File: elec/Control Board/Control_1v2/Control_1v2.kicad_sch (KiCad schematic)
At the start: 170 parts, among them J1 DB9_Female_MountingHoles, J10 Conn_02x12_Odd_Even, J11 Con_01x02_2.5mm, J14 Conn_01x10, J2 Conn_01x08, J25 Con_01x02_2.5mm, J26 Conn_01x10, J27 Conn_02x12_Odd_Even, J28 Con_01x02_2.5mm, J29 Conn_01x10, J3 Conn_01x08, J37 Conn_01x04, J4 Conn_01x08, J5 Conn_01x08, J6 Conn_01x08, J7 Conn_01x10, J8 Conn_02x18_Odd_Even, J9 Conn_01x10, Q601 BSS138

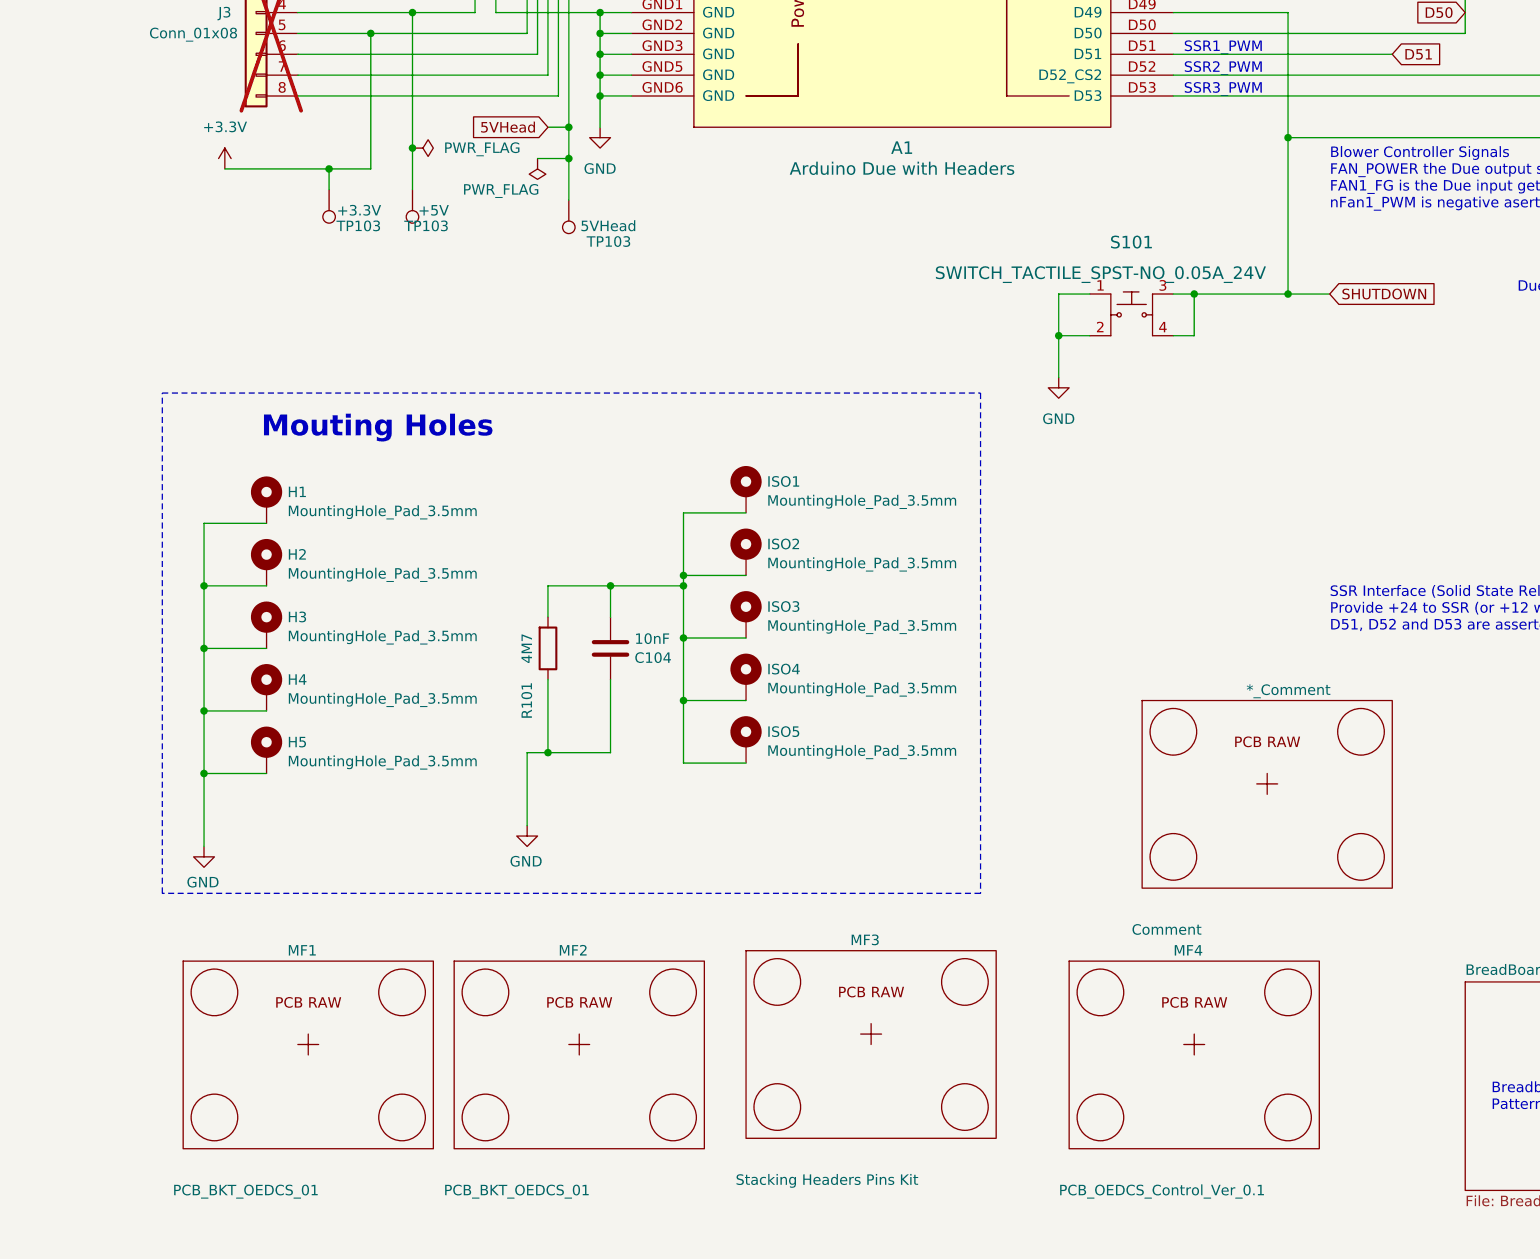
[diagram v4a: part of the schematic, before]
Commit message: Add a connector next to the SHUTDOWN switch. Add 3D file for relay.
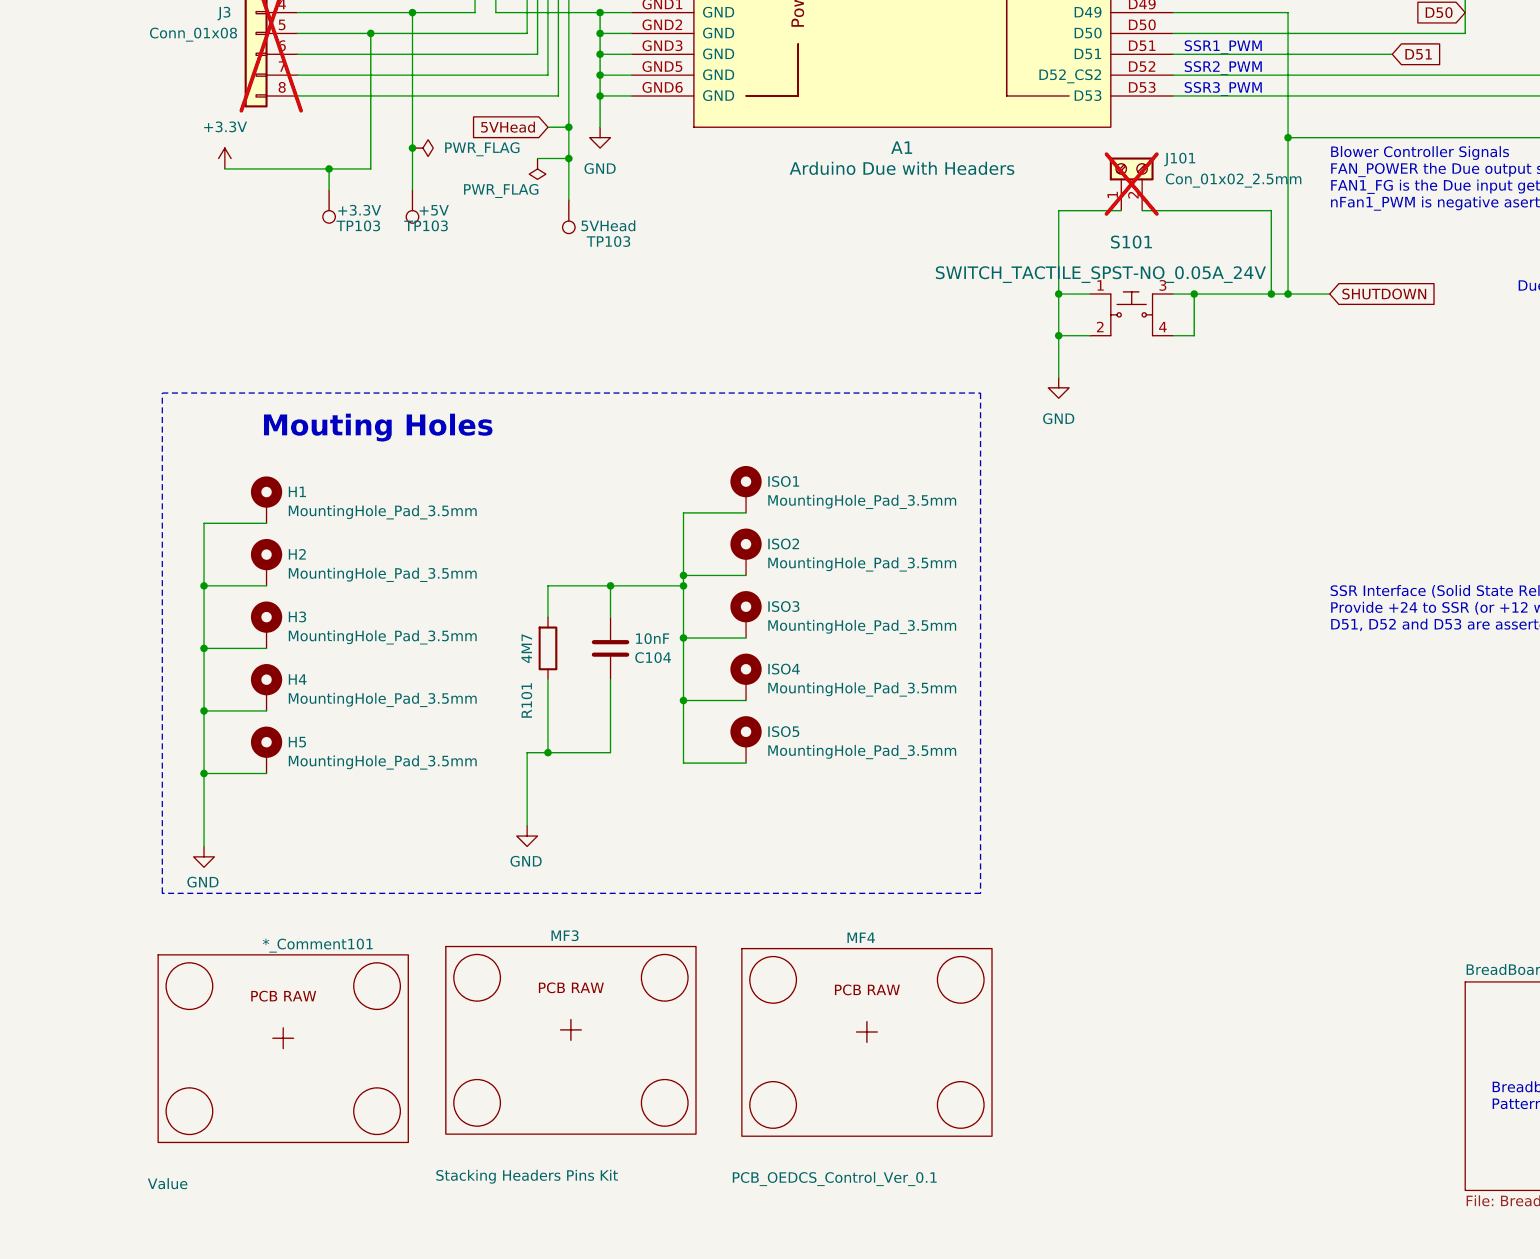
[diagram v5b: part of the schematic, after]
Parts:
- removed MF1, MF2: PCB_BKT_OEDCS_01, NA, symbol GPAD_SCH_LIB:PCB_GPAD_VER1
- added J101: Con_01x02_2.5mm, PubInv_KiCad_PCB:JST_XH_B2B-XH-AM_1x02_P2.50mm_Vertical, symbol Connector:Screw_Terminal_01x02
- *_Comment101: renamed from *_Comment; value Comment -> Value
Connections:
- net GND: now also J101.1 (Pin_1)
- net SHUTDOWN: now also J101.2 (Pin_2)
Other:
- moved on the sheet: *_Comment101, MF3, MF4

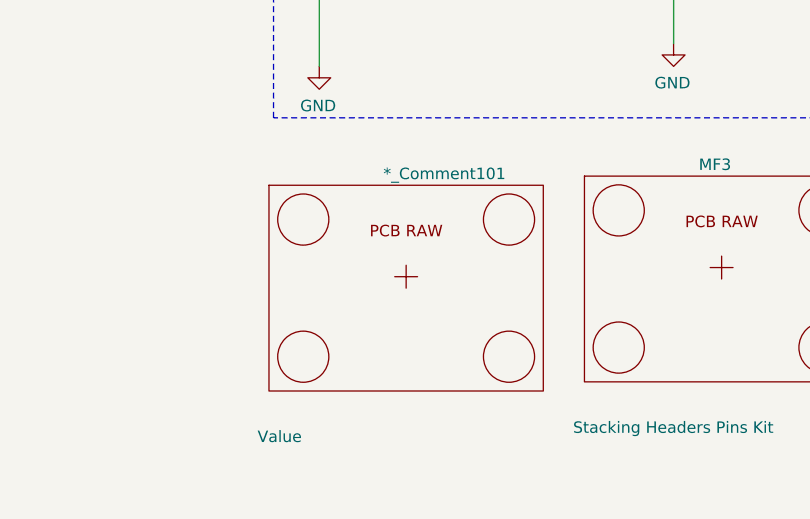
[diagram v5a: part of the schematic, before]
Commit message: PCB V1.2. Fixes to parts for BOM and PL.
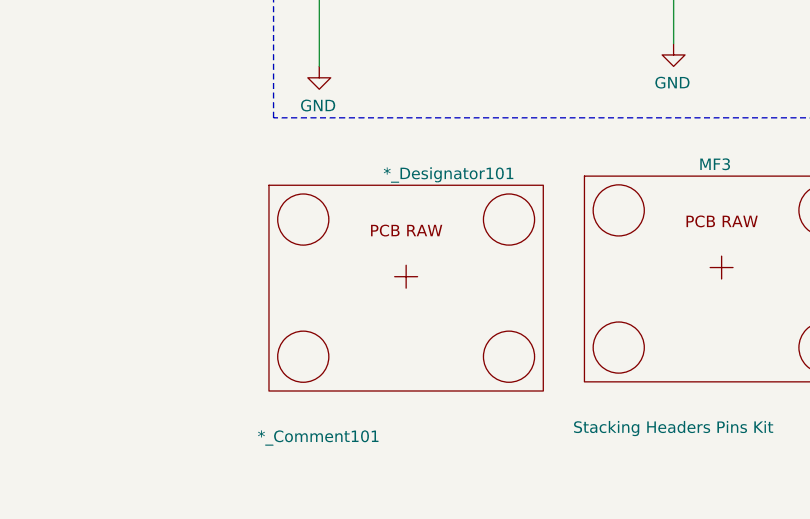
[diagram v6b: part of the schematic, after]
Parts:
- *_Designator101: renamed from *_Comment101; value Value -> *_Comment101
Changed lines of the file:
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@@
   (symbol (lib_id "GPAD_SCH_LIB:PCB_GPAD_VER1") (at 174.752 290.068 0) (unit 1)
     (in_bom yes) (on_board no) (dnp no)
-    (property "Reference" "*_Comment101" (at 172.212 278.638 0)
+    (property "Reference" "*_Designator101" (at 172.212 278.638 0)
       (effects (font (size 1.27 1.27)) (justify left))
     )
-    (property "Value" "Value" (at 158.242 307.848 0)
+    (property "Value" "*_Comment101" (at 158.242 307.848 0)
       (effects (font (size 1.27 1.27)) (justify left))
     )
@@
       (project "Control_1v2"
         (path "/c68c9deb-8d4d-42f0-adf8-4d3022f4ee59"
-          (reference "*_Comment101") (unit 1)
+          (reference "*_Designator101") (unit 1)
         )
       )

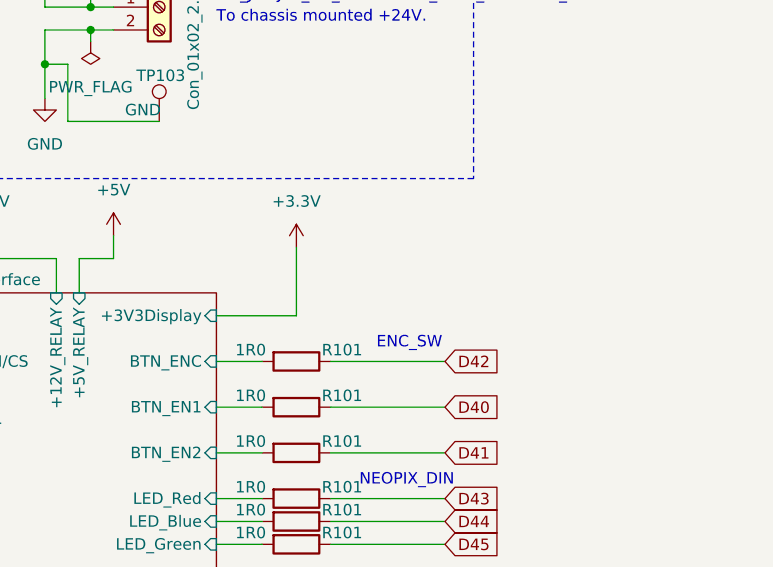
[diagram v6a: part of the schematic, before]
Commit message: Update schematic with new resistor R186 required for front panel switch.
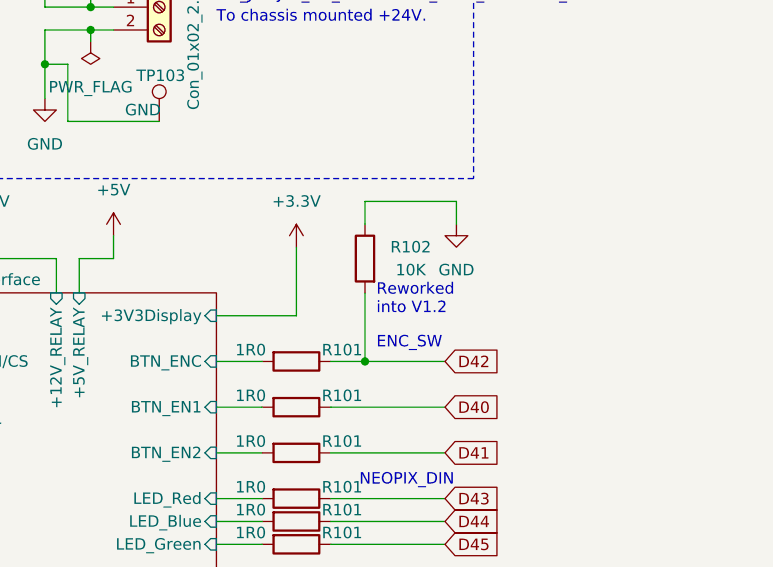
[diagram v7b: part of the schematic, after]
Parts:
- added R102: 10K, Resistor_SMD:R_0603_1608Metric_Pad0.98x0.95mm_HandSolder, symbol Device:R
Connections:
- net D42: now also R102.2
- net GND: now also R102.1
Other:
- note added: "Reworked into V1.2"
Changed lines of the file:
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@@
   (junction (at 213.36 167.64) (diameter 0) (color 0 0 0 0)
   )
+  (junction (at 505.46 246.38) (diameter 0) (color 0 0 0 0)
+  )
   (junction (at 477.52 132.08) (diameter 0) (color 0 0 0 0)
   )
@@
     (stroke (width 0) (type default))
   )
+  (wire (pts (xy 515.62 228.6) (xy 505.46 228.6))
+    (stroke (width 0) (type default))
+  )
   (wire (pts (xy 426.72 50.8) (xy 424.18 50.8))
     (stroke (width 0) (type default))
@@
     (stroke (width 0) (type default))
   )
+  (wire (pts (xy 505.46 228.6) (xy 505.46 231.14))
+    (stroke (width 0) (type default))
+  )
   (wire (pts (xy 463.55 91.44) (xy 463.55 114.3))
     (stroke (width 0) (type default))
@@
     (stroke (width 0) (type default))
   )
-  (wire (pts (xy 514.35 246.38) (xy 501.65 246.38))
+  (wire (pts (xy 514.35 246.38) (xy 505.46 246.38))
     (stroke (width 0) (type default))
   )
@@
     (stroke (width 0) (type default))
   )
+  (wire (pts (xy 515.62 231.14) (xy 515.62 228.6))
+    (stroke (width 0) (type default))
+  )
   (wire (pts (xy 477.52 127) (xy 455.93 127))
     (stroke (width 0) (type default))
@@
     (stroke (width 0) (type default))
   )
+  (wire (pts (xy 505.46 246.38) (xy 501.65 246.38))
+    (stroke (width 0) (type default))
+  )
   (wire (pts (xy 448.31 246.38) (xy 454.66 246.38))
     (stroke (width 0) (type default))
@@
     (stroke (width 0) (type default))
   )
+  (wire (pts (xy 505.46 238.76) (xy 505.46 246.38))
+    (stroke (width 0) (type default))
+  )
   (wire (pts (xy 433.07 49.53) (xy 426.72 49.53))
     (stroke (width 0) (type default))
@@
     (effects (font (size 1.27 1.27)) (justify left bottom))
   )
+  (text "Reworked \ninto V1.2" (at 506.73 241.3 0)
+    (effects (font (size 1.27 1.27)) (justify left bottom))
+  )
   (text "V_ASSY_VERSIONING\nControl 1.2 voltage = 1.055V" (at 124.714 137.414 0)
     (effects (font (size 1.27 1.27)) (justify left bottom))
@@
     )
   )
+  (symbol (lib_id "Device:R") (at 505.46 234.95 0) (mirror y) (unit 1)
+    (in_bom yes) (on_board yes) (dnp no)
+    (property "Reference" "R102" (at 510.54 233.68 0)
+      (effects (font (size 1.27 1.27)))
+    )
+    (property "Value" "10K" (at 510.54 236.22 0)
+      (effects (font (size 1.27 1.27)))
+    )
+    (property "Footprint" "Resistor_SMD:R_0603_1608Metric_Pad0.98x0.95mm_HandSolder" (at 507.238 234.95 90)
+      (effects (font (size 1.27 1.27)) hide)
+    )
+    (property "Datasheet" "https://datasheet.lcsc.com/lcsc/1811101310_TyoHM-RMC06031K1-N_C269704.pdf" (at 505.46 234.95 0)
+      (effects (font (size 1.27 1.27)) hide)
+    )
+    (property "Distributor 1" "JLCPCB" (at 505.46 234.95 90)
+      (effects (font (size 1.27 1.27)) hide)
+    )
+    (property "Distributor 1 PN" "C269701" (at 505.46 234.95 90)
+      (effects (font (size 1.27 1.27)) hide)
+    )
+    (property "Manufacturer" "TyoHM" (at 505.46 234.95 90)
+      (effects (font (size 1.27 1.27)) hide)
+    )
+    (property "MPN" "RMC060310KFN" (at 505.46 234.95 90)
+      (effects (font (size 1.27 1.27)) hide)
+    )
+    (property "Description" "100mW ±1% 10kΩ 0603 Chip Resistor - Surface Mount ROHS" (at 505.46 234.95 0)
+      (effects (font (size 1.27 1.27)) hide)
+    )
+    (property "AssemblyType" "SMT" (at 505.46 234.95 0)
+      (effects (font (size 1.27 1.27)) hide)
+    )
+    (property "Cost" "0.0015" (at 505.46 234.95 0)
+      (effects (font (size 1.27 1.27)) hide)
+    )
+    (property "LongLead" "NO" (at 505.46 234.95 0)
+      (effects (font (size 1.27 1.27)) hide)
+    )
+    (pin "1")
+    (pin "2")
+    (instances
+      (project "GeneralPurposeAlarmDevicePCB"
+        (path "/412a327d-1ee3-473e-bc00-1545004b7edf"
+          (reference "R102") (unit 1)
+        )
+      )
+      (project "Control_1v2"
+        (path "/c68c9deb-8d4d-42f0-adf8-4d3022f4ee59/0cb2f0dc-fe38-451d-b752-5d12a98f8d03"
+          (reference "R41") (unit 1)
+        )
+        (path "/c68c9deb-8d4d-42f0-adf8-4d3022f4ee59"
+          (reference "R186") (unit 1)
+        )
+      )
+    )
+  )
   (symbol (lib_id "Device:R") (at 80.01 285.75 180) (unit 1)
     (in_bom yes) (on_board yes) (dnp no)
@@
         )
       )
+    )
+  )
+  (symbol (lib_id "power:GND") (at 515.62 231.14 0) (unit 1)
+    (in_bom yes) (on_board yes) (dnp no) (fields_autoplaced)
+    (property "Reference" "#PWR0113" (at 515.62 237.49 0)
+      (effects (font (size 1.27 1.27)) hide)
+    )
+    (property "Value" "GND" (at 515.62 236.22 0)
+      (effects (font (size 1.27 1.27)))
+    )
+    (property "Footprint" "" (at 515.62 231.14 0)
+      (effects (font (size 1.27 1.27)) hide)
+    )
+    (property "Datasheet" "" (at 515.62 231.14 0)
+      (effects (font (size 1.27 1.27)) hide)
+    )
+    (pin "1")
+    (instances
+      (project "Control_1v2"
+        (path "/c68c9deb-8d4d-42f0-adf8-4d3022f4ee59"
+          (reference "#PWR0113") (unit 1)
+        )
+      )

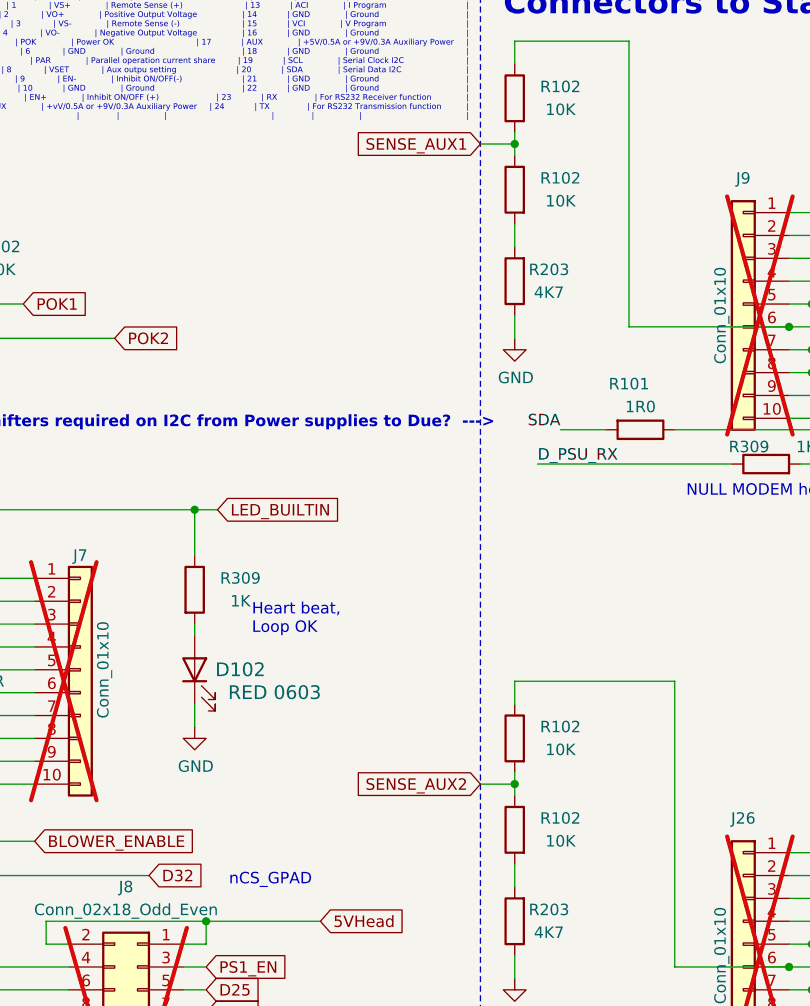
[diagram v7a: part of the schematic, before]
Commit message: Update DueWithThreeSSRs.ino for new resistive dividers. Add notes for same on schematic.
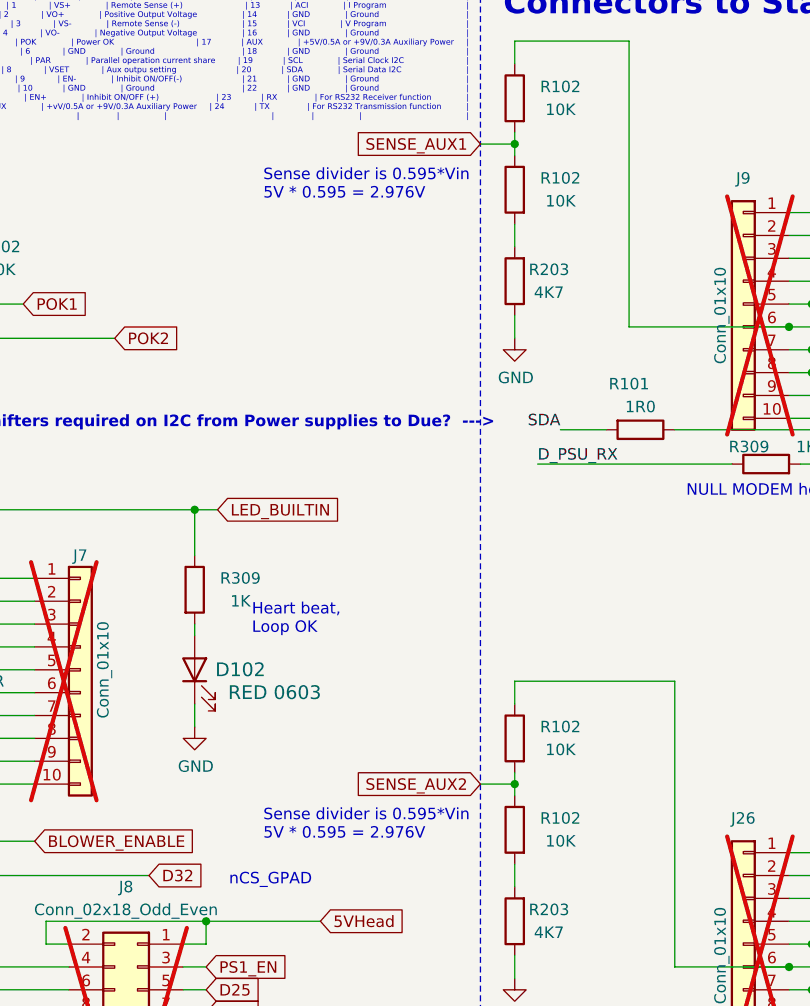
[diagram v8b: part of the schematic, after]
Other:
- note added: "Sense divider is 0.595*Vin 5V * 0.595 = 2.976V"
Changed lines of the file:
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@@
     (effects (font (size 2.54 2.54)) (justify left bottom))
+  )
+  (text "Sense divider is 0.595*Vin\n5V * 0.595 = 2.976V" (at 365.76 39.37 0)
+    (effects (font (size 1.27 1.27)) (justify left bottom))
   )
   (text "Connector_JST:JST_XH_B2B-XH-AM_1x02_P2.50mm_Vertical\n"
@@
     (effects (font (size 1.27 1.27)) (justify left bottom))
   )
+  (text "Sense divider is 0.595*Vin\n5V * 0.595 = 2.976V" (at 365.76 110.49 0)
+    (effects (font (size 1.27 1.27)) (justify left bottom))
+  )
